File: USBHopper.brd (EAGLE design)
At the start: 81.2 x 20.3 mm, 42 parts, among them Q1 2.5A/30V, U2 4k7/47k, U3 4k7/47k, U4 DCDC, U5 DCDC, X1 USB-1X-2S-PLUG-A-SMD

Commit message: LED beschriftungen
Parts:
- renumbered PWRLED to LED2, RXLED to LED3, SENSE to LED1, TXLED to LED4
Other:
- board text added: "LED1"
- board text added: "LED2"
- board text added: "LED3"
- board text added: "LED4"
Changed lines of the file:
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@@
 <text x="47.752" y="2.032" size="0.6096" layer="51" font="vector" ratio="16" distance="175" rot="R90">R3</text>
 <text x="59.817" y="2.032" size="0.6096" layer="51" font="vector" ratio="16" distance="175" rot="R90">R4</text>
-<text x="57.531" y="17.272" size="0.6096" layer="51" font="vector" ratio="16" distance="175" rot="R90">R5</text>
-<text x="45.593" y="17.399" size="0.6096" layer="51" font="vector" ratio="16" distance="175" rot="R90">R6</text>
+<text x="59.817" y="17.272" size="0.6096" layer="51" font="vector" ratio="16" distance="175" rot="R90">R5</text>
+<text x="47.752" y="17.272" size="0.6096" layer="51" font="vector" ratio="16" distance="175" rot="R90">R6</text>
 <text x="11.557" y="7.112" size="0.6096" layer="51" font="vector" ratio="16" distance="175" rot="R90">C1</text>
 <text x="17.907" y="8.763" size="0.6096" layer="51" font="vector" ratio="16" distance="175">C2</text>
@@
 <wire x1="25.4" y1="0.508" x2="25.654" y2="0.508" width="0.1524" layer="51"/>
 <wire x1="27.94" y1="0.508" x2="27.686" y2="0.508" width="0.1524" layer="51"/>
+<text x="50.292" y="1.651" size="0.6096" layer="51" font="vector" ratio="16" distance="175" rot="R90">LED1</text>
+<text x="62.357" y="1.524" size="0.6096" layer="51" font="vector" ratio="16" distance="175" rot="R90">LED2</text>
+<text x="50.292" y="16.764" size="0.6096" layer="51" font="vector" ratio="16" distance="175" rot="R90">LED3</text>
+<text x="62.357" y="16.764" size="0.6096" layer="51" font="vector" ratio="16" distance="175" rot="R90">LED4</text>
 </plain>
 <attributes>
@@
 </element>
 <element name="X1" library="con-usb" package="USB-PLUG-A-SMD-2S" value="USB-1X-2S-PLUG-A-SMD" x="-4.445" y="10.16"/>
-<element name="PWRLED" library="flo-led" package="KPT-2012" value="Blue" x="60.96" y="2.54" rot="R180"/>
+<element name="LED2" library="flo-led" package="KPT-2012" value="Blue" x="60.96" y="2.54" rot="R180"/>
 <element name="HGND" library="pinhead" package="1X02" value="" x="26.67" y="18.415"/>
 <element name="C6" library="flo-parts" package="0805" value="4.4µF" x="10.16" y="17.145" rot="R270"/>
@@
 <element name="L3" library="flo-parts" package="0806" value="2.2µH &lt;- check" x="19.05" y="3.175" rot="R270"/>
 <element name="C9" library="flo-parts" package="0805" value="10µF &lt;- check" x="21.59" y="3.175" rot="R90"/>
-<element name="SENSE" library="flo-led" package="KPT-2012" value="Orange" x="48.895" y="2.54" rot="R180"/>
+<element name="LED1" library="flo-led" package="KPT-2012" value="Orange" x="48.895" y="2.54" rot="R180"/>
 <element name="U4" library="flo-parts" package="SOT23" value="DCDC" x="14.605" y="17.145" rot="R270"/>
 <element name="U5" library="flo-parts" package="SOT23" value="DCDC" x="14.605" y="3.175" rot="R270"/>
-<element name="TXLED" library="flo-led" package="KPT-2012" value="Green" x="60.96" y="17.78" rot="R180"/>
-<element name="RXLED" library="flo-led" package="KPT-2012" value="Red" x="48.895" y="17.78" rot="R180"/>
+<element name="LED4" library="flo-led" package="KPT-2012" value="Green" x="60.96" y="17.78" rot="R180"/>
+<element name="LED3" library="flo-led" package="KPT-2012" value="Red" x="48.895" y="17.78" rot="R180"/>
 <element name="JTX" library="flo-parts" package="0805_CONNECT" value="" x="61.595" y="17.78" rot="MR270"/>
 <element name="JRX" library="flo-parts" package="0805_CONNECT" value="" x="49.53" y="17.78" rot="MR90"/>
@@
 <contactref element="U3" pad="P$6"/>
 <contactref element="U1" pad="P$6"/>
-<contactref element="PWRLED" pad="2"/>
+<contactref element="LED2" pad="2"/>
 <contactref element="C9" pad="P$1"/>
 <contactref element="C8" pad="P$2"/>
@@
 </signal>
 <signal name="N$1">
-<contactref element="PWRLED" pad="1"/>
+<contactref element="LED2" pad="1"/>
 <contactref element="R4" pad="P$1"/>
 <wire x1="60.96" y1="3.44" x2="58.454" y2="3.59" width="0.1524" layer="1"/>
@@
 </signal>
 <signal name="N$2">
-<contactref element="SENSE" pad="1"/>
+<contactref element="LED1" pad="1"/>
 <contactref element="R3" pad="P$1"/>
 <wire x1="48.895" y1="3.44" x2="46.389" y2="1.49" width="0.1524" layer="1"/>
@@
 </signal>
 <signal name="SENSLED">
-<contactref element="SENSE" pad="2"/>
+<contactref element="LED1" pad="2"/>
 <contactref element="U1" pad="P$1"/>
 <wire x1="52.959" y1="1.651" x2="52.959" y2="2.413" width="0.1524" layer="1"/>
@@
 </signal>
 <signal name="N$10">
-<contactref element="TXLED" pad="2"/>
+<contactref element="LED4" pad="2"/>
 <contactref element="JTX" pad="P$1"/>
 <contactref element="U2" pad="P$1"/>
@@
 </signal>
 <signal name="N$11">
-<contactref element="TXLED" pad="1"/>
+<contactref element="LED4" pad="1"/>
 <contactref element="R5" pad="P$1"/>
 <wire x1="60.96" y1="18.68" x2="60.74" y2="19.05" width="0.1524" layer="1"/>
@@
 </signal>
 <signal name="N$6">
-<contactref element="RXLED" pad="2"/>
+<contactref element="LED3" pad="2"/>
 <contactref element="JRX" pad="P$1"/>
 <contactref element="U3" pad="P$1"/>
@@
 </signal>
 <signal name="N$12">
-<contactref element="RXLED" pad="1"/>
+<contactref element="LED3" pad="1"/>
 <contactref element="R6" pad="P$1"/>
 <wire x1="48.895" y1="18.68" x2="48.675" y2="19.05" width="0.1524" layer="1"/>

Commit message: The downside is the upside.
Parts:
- added R10, R11, R12, R9: 0, flo-parts:0805_CONNECT
- added R7: 60, flo-parts:0805
- added R8: 60, flo-parts:0805_CONNECT
- added U$10, U$11, U$4, U$5: CON1X1PIN_XL, flo-header:1X1PINS
- added U$20: TANTAL1206, flo-parts:1206
- C5: value 4.7µF -> 220pF; device rcl:153CLV-0405 -> flo-parts:0805
- C6: value 4.4µF -> 4.7µF
- C7: value 4.4µF <- check -> 4.7µF
- C9: value 10µF <- check -> 10µF
- JRX, JTX: value (none) -> 0
- L2: value 2.2µH -> 1.0µH
- L3: value 2.2µH <- check -> 1.0µH
- R4: value 270 -> 330
- U1: value (none) -> 4k7/47k
- U4: value DCDC -> ADP2108AUJZ-3.3-R7
- U5: value DCDC -> ADP2108AUJZ-1.8-R7
- moved C5 23.7 mm to (55.9, 1.91), flipped to the bottom, turned to 270 degrees
- moved C4 1.17 mm to (28.8, 10.1)
- moved L1 1.01 mm to (9.16, 11.9)
- moved L3 1.00 mm to (18.1, 3.23), turned to 90 degrees
- moved C1 1.00 mm to (9.16, 7.62)
- moved C2 1.00 mm to (17.4, 10.2)
- moved C3 1.00 mm to (49.2, 10.2)
- moved C6 1.00 mm to (9.16, 17.1)
- moved C7 1.00 mm to (9.16, 3.17)
- moved C8 1.00 mm to (20.6, 17.1)
- moved C9 1.00 mm to (20.6, 3.17)
- moved FTDI 1.00 mm to (56.1, 10.2)
- moved HGND 1.00 mm to (25.7, 18.4)
- moved JPWRSEL 1.00 mm to (23.8, 10.2)
- moved JRX 1.00 mm to (48.5, 17.8)
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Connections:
- removed net RX: U3.P$5
- removed net TX: U2.P$5
- removed net U3: U3.P$2, U3.P$3
- new net DE: R10.P$2, RS485.3, U$57.P$3
- new net N$5: L2.P$2, U4.P5
- new net RE#: R9.P$2, RS485.2, U$57.P$2
- new net SEN3: U$10.P$1, U2.P$2, U2.P$3
- new net SEN4: U$11.P$1, U3.P$2, U3.P$3
- net +1V8: now also U5.P4; no longer U5.P5
- net +3V3: now also R11.P$2, U4.P4; no longer U4.P5
- net +5V: now also R12.P$2, U$4.P$1; no longer RS485.8, U$57.P$8
- net GND: now also C5.P$2, U$20.P$2, U$5.P$1; no longer C5.-
- net N$7: now also U5.P5; no longer U5.P4
- net N$8: now also C5.P$1, R7.P$1, R8.P$1; no longer L2.P$2, U4.P4
- net N$9: now also R11.P$1, R12.P$1, RS485.8, U$57.P$8; no longer U2.P$2, U2.P$3
- net PWREN#: now also R9.P$1; no longer RS485.2, U$57.P$2
- net RS485A: now also R7.P$2
- net RS485B: now also R8.P$2
- net RXD: now also U3.P$5
- net TXD: now also U2.P$5
- net TXDEN: now also R10.P$1; no longer RS485.3, U$57.P$3
- net USB+5V: now also U$20.P$1; no longer C5.+
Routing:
- net RXD: track 73.5 -> 97.9 mm, vias 2 -> 8
- net FSM: track 0.00 -> 17.1 mm
- net RE#: track 0.00 -> 12.2 mm, vias 0 -> 2
- net TXD: track 71.8 -> 83.3 mm, vias 4 -> 6
- net N$9: track 0.90 -> 10.3 mm, vias 0 -> 1
- net TXDEN: track 55.4 -> 46.5 mm, vias 4 -> 3
- net DE: track 0.00 -> 8.36 mm, vias 0 -> 1
- net PWREN#: track 92.6 -> 85.0 mm, vias 7 -> 6
- net SEN3: track 0.00 -> 5.95 mm
- net SEN4: track 0.00 -> 5.71 mm
- net N$8: track 2.92 -> 6.23 mm
- net +3V3: track 21.9 -> 25.0 mm, vias 0 -> 1
- net RS485B: track 54.7 -> 57.7 mm, vias 2 -> 4
- net N$5: track 0.00 -> 2.96 mm
- net GND: track 51.5 -> 54.2 mm
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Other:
- board size 81.2 x 20.3 mm -> 80 x 20.3 mm
- board text added: "#"
- board text added: "30°"
- board text added: "45°"
- board text added: "6"
- board text added: "60°"
- board text added: "7"
- board text added: "A"
- board text added: "B"
- board text added: "BOTTOM"
- board text added: "BSILK"
- board text added: "BSTOP"
- board text added: "C"
- board text added: "C=---"
- board text added: "CT"
- board text added: "D"
- board text added: "DE"
- board text added: "E"
- board text added: "G"
- board text added: "I"
- board text added: "I t"
- board text added: "K"
- board text added: "NPN"
- board text added: "PE"
- board text added: "Pch"
- board text added: "R=-"
- board text added: "RE"
- board text added: "RT"
- board text added: "TE"
- board text added: "TOP"
- board text added: "TSILK"
- board text added: "TSTOP"
- board text added: "U"
- board text added: "rxled"
- board text added: "term"
- board text added: "txled"

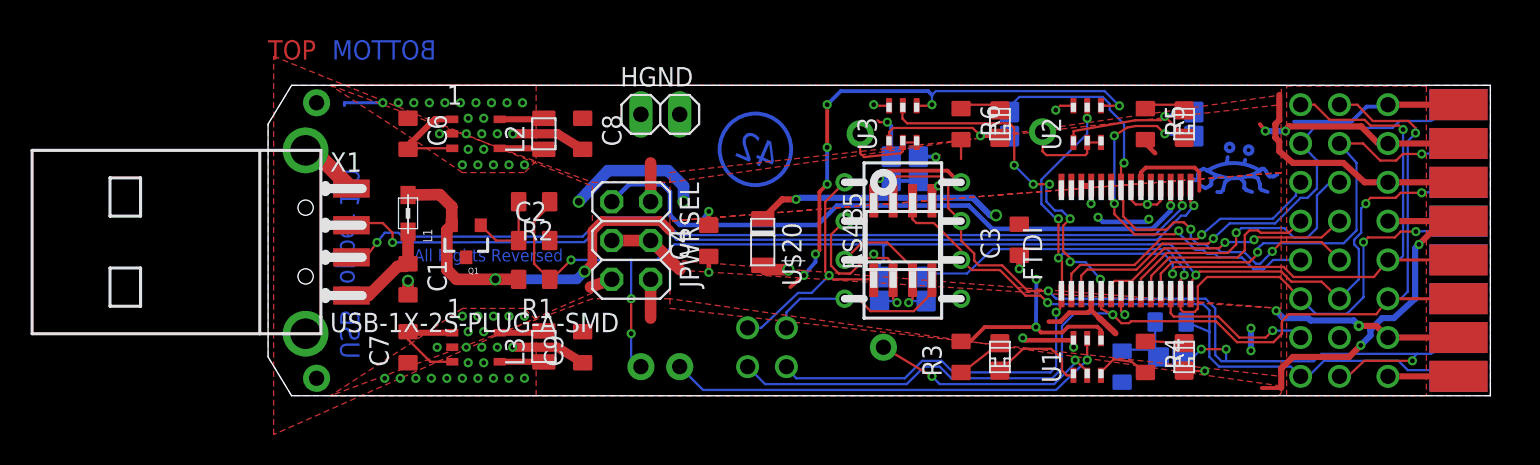
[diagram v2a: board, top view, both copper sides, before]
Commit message: Bugfixes. Pad auf GND.
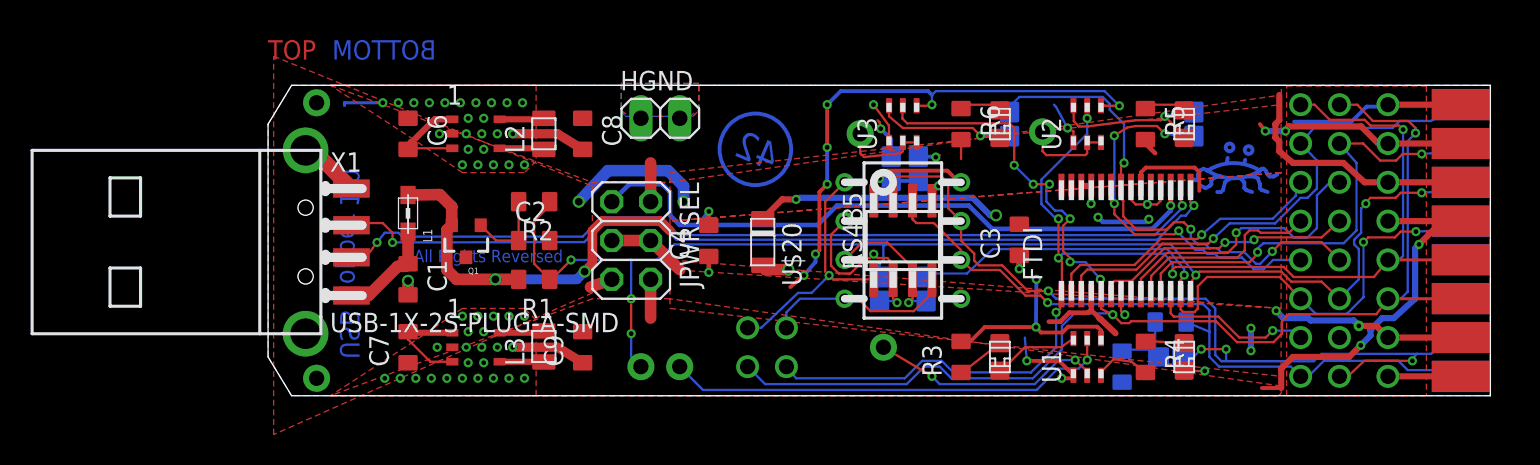
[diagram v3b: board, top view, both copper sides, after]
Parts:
- moved HGND 0.25 mm to (25.7, 18.2)
- moved U$66 0.15 mm to (80.0, 10.2)
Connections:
- removed net SENSLED: LED1.2, U1.P$1
- new net N$15: LED1.2, U1.P$6
- net GND: now also U1.P$1, U2.P$1, U3.P$1; no longer U1.P$6, U2.P$6, U3.P$6
- net N$10: now also U2.P$6; no longer U2.P$1
- net N$6: now also U3.P$6; no longer U3.P$1
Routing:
- net SENSLED: track 6.53 -> 0.00 mm
- net N$15: track 0.00 -> 5.64 mm
- net GND: track 54.2 -> 59.2 mm
- net TXD: track 83.3 -> 82.7 mm
- net RXD: track 97.9 -> 97.3 mm

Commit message: V1.0
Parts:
- removed U$21: CON1X1PIN_XL, flo-header:1X1PINS
- added S1: CON1X1PIN_XL, flo-header:1X1PINS
- LED1, LED2, LED3, LED4: device flo-led:KPT-2012 -> flo-led:KPT-2012-E
- renumbered U$10 to S4, U$11 to S3, U$27 to S2
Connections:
- net SENSE: now also S1.P$1; no longer U$21.P$1
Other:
- board text added: "V1.1"
